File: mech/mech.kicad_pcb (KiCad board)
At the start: 2 copper layers, 53.3 x 78.7 mm, 28 parts, among them P1 Pump_Motor_DC, P2 Pump_Motor_DC, T1 DS18B20, T2 DS18B20, U1 DHT22

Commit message: fix edge corner
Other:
- outline, holes or cut-outs redrawn
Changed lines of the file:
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@@
   )
   (layers
-    (0 F.Cu signal hide)
-    (31 B.Cu signal hide)
+    (0 F.Cu signal)
+    (31 B.Cu signal)
     (32 B.Adhes user)
     (33 F.Adhes user)
@@
       (outputformat 1)
       (mirror false)
-      (drillshape 1)
+      (drillshape 0)
       (scaleselection 1)
       (outputdirectory ""))
@@
     )
   )
+  (gr_arc (start 86.36 184.15) (end 81.28 184.15) (angle -90) (layer Edge.Cuts) (width 0.05))
+  (gr_line (start 129.54 189.23) (end 86.36 189.23) (layer Edge.Cuts) (width 0.05))
+  (gr_line (start 134.62 115.57) (end 134.62 184.15) (layer Edge.Cuts) (width 0.05))
+  (gr_line (start 86.36 110.49) (end 129.54 110.49) (layer Edge.Cuts) (width 0.05))
+  (gr_line (start 81.28 184.15) (end 81.28 115.57) (layer Edge.Cuts) (width 0.05))
+  (gr_arc (start 86.36 115.57) (end 86.36 110.49) (angle -90) (layer Edge.Cuts) (width 0.05))
+  (gr_arc (start 129.54 184.15) (end 129.54 189.23) (angle -90) (layer Edge.Cuts) (width 0.05))
+  (gr_arc (start 129.54 115.57) (end 134.62 115.57) (angle -90) (layer Edge.Cuts) (width 0.05))
   (dimension 78.74 (width 0.12) (layer B.SilkS)
-    (gr_text "78,740 mm" (at 143.51 149.86 90) (layer B.SilkS)
-      (effects (font (size 1 1) (thickness 0.15)))
-    )
-    (feature1 (pts (xy 130.81 110.49) (xy 142.826421 110.49)))
-    (feature2 (pts (xy 130.81 189.23) (xy 142.826421 189.23)))
-    (crossbar (pts (xy 142.24 189.23) (xy 142.24 110.49)))
-    (arrow1a (pts (xy 142.24 110.49) (xy 142.826421 111.616504)))
-    (arrow1b (pts (xy 142.24 110.49) (xy 141.653579 111.616504)))
-    (arrow2a (pts (xy 142.24 189.23) (xy 142.826421 188.103496)))
-    (arrow2b (pts (xy 142.24 189.23) (xy 141.653579 188.103496)))
+    (gr_text "78,740 mm" (at 142.24 149.86 90) (layer B.SilkS)
+      (effects (font (size 1 1) (thickness 0.15)))
+    )
+    (feature1 (pts (xy 129.54 110.49) (xy 141.556421 110.49)))
+    (feature2 (pts (xy 129.54 189.23) (xy 141.556421 189.23)))
+    (crossbar (pts (xy 140.97 189.23) (xy 140.97 110.49)))
+    (arrow1a (pts (xy 140.97 110.49) (xy 141.556421 111.616504)))
+    (arrow1b (pts (xy 140.97 110.49) (xy 140.383579 111.616504)))
+    (arrow2a (pts (xy 140.97 189.23) (xy 141.556421 188.103496)))
+    (arrow2b (pts (xy 140.97 189.23) (xy 140.383579 188.103496)))
   )
   (dimension 53.34 (width 0.12) (layer B.SilkS)
-    (gr_text "53,340 mm" (at 107.95 196.215) (layer B.SilkS)
-      (effects (font (size 1 1) (thickness 0.15)))
-    )
-    (feature1 (pts (xy 134.62 185.42) (xy 134.62 195.531421)))
-    (feature2 (pts (xy 81.28 185.42) (xy 81.28 195.531421)))
-    (crossbar (pts (xy 81.28 194.945) (xy 134.62 194.945)))
-    (arrow1a (pts (xy 134.62 194.945) (xy 133.493496 195.531421)))
-    (arrow1b (pts (xy 134.62 194.945) (xy 133.493496 194.358579)))
-    (arrow2a (pts (xy 81.28 194.945) (xy 82.406504 195.531421)))
-    (arrow2b (pts (xy 81.28 194.945) (xy 82.406504 194.358579)))
-  )
-  (gr_line (start 130.925 110.49) (end 85.205 110.49) (layer Edge.Cuts) (width 0.05))
-  (gr_arc (start 85.09 114.3) (end 85.09 110.49) (angle -90) (layer Edge.Cuts) (width 0.05))
-  (gr_line (start 81.28 185.42) (end 81.28 114.3) (layer Edge.Cuts) (width 0.05))
-  (gr_line (start 130.81 189.23) (end 85.09 189.23) (layer Edge.Cuts) (width 0.05))
-  (gr_arc (start 130.81 185.42) (end 130.81 189.23) (angle -90) (layer Edge.Cuts) (width 0.05))
-  (gr_line (start 134.62 114.3) (end 134.62 185.42) (layer Edge.Cuts) (width 0.05))
-  (gr_arc (start 130.81 114.3) (end 134.62 114.3) (angle -90) (layer Edge.Cuts) (width 0.05))
-  (gr_arc (start 85.09 185.42) (end 81.28 185.42) (angle -90) (layer Edge.Cuts) (width 0.05))
-  (gr_text contact@yasiu.pl (at 108.065 186.055) (layer F.SilkS)
+    (gr_text "53,340 mm" (at 107.95 194.945) (layer B.SilkS)
+      (effects (font (size 1 1) (thickness 0.15)))
+    )
+    (feature1 (pts (xy 134.62 184.15) (xy 134.62 194.261421)))
+    (feature2 (pts (xy 81.28 184.15) (xy 81.28 194.261421)))
+    (crossbar (pts (xy 81.28 193.675) (xy 134.62 193.675)))
+    (arrow1a (pts (xy 134.62 193.675) (xy 133.493496 194.261421)))
+    (arrow1b (pts (xy 134.62 193.675) (xy 133.493496 193.088579)))
+    (arrow2a (pts (xy 81.28 193.675) (xy 82.406504 194.261421)))
+    (arrow2b (pts (xy 81.28 193.675) (xy 82.406504 193.088579)))
+  )
+  (gr_text contact@yasiu.pl (at 108.065 184.785) (layer F.SilkS)
     (effects (font (size 1 1) (thickness 0.15)))
   )

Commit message: add JLC part number stub
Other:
- board text added: "JLCJLCJLCJLC"
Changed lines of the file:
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@@
   (general
     (thickness 1.6)
-    (drawings 13)
+    (drawings 14)
     (tracks 72)
     (zones 0)
@@
     )
   )
+  (gr_text JLCJLCJLCJLC (at 107.95 184.15) (layer B.SilkS)
+    (effects (font (size 1 1) (thickness 0.15)) (justify mirror))
+  )
   (gr_arc (start 86.36 184.15) (end 81.28 184.15) (angle -90) (layer Edge.Cuts) (width 0.05))

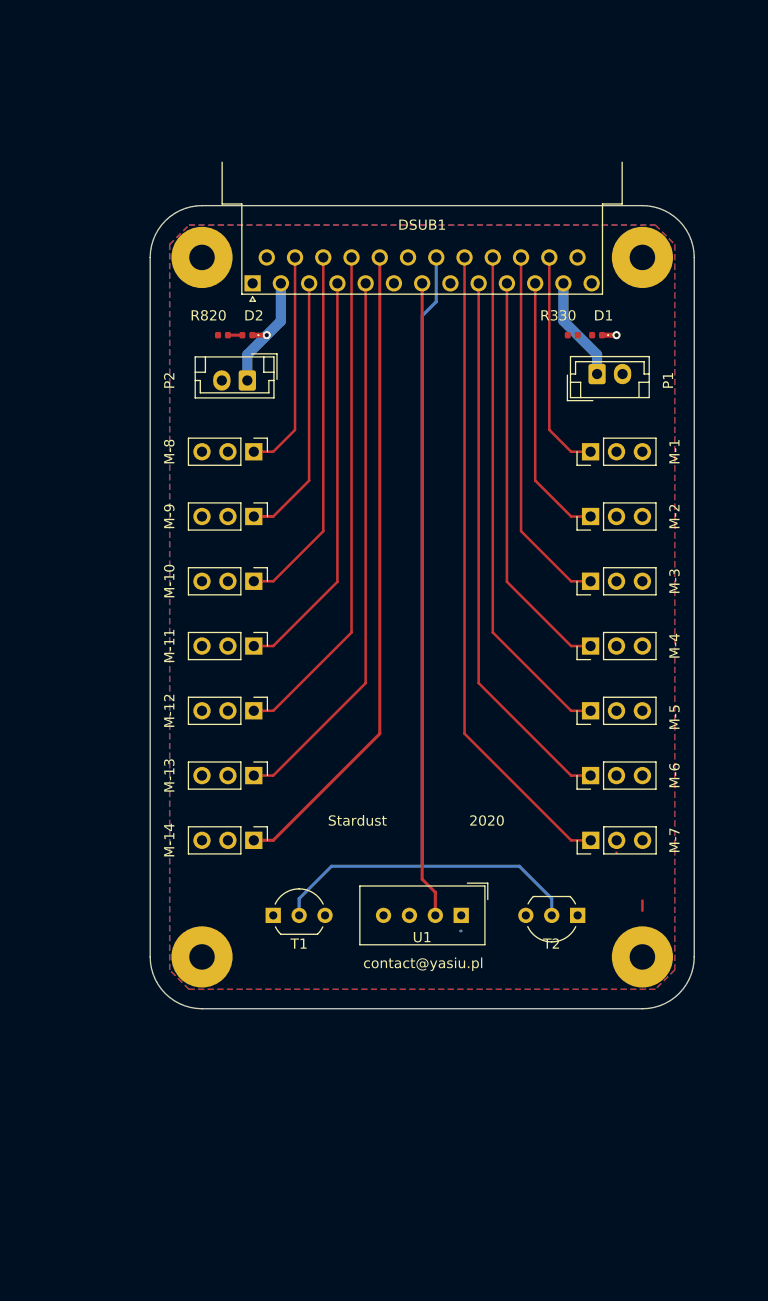
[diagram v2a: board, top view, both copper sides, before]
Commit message: ADC + PCA9685 version
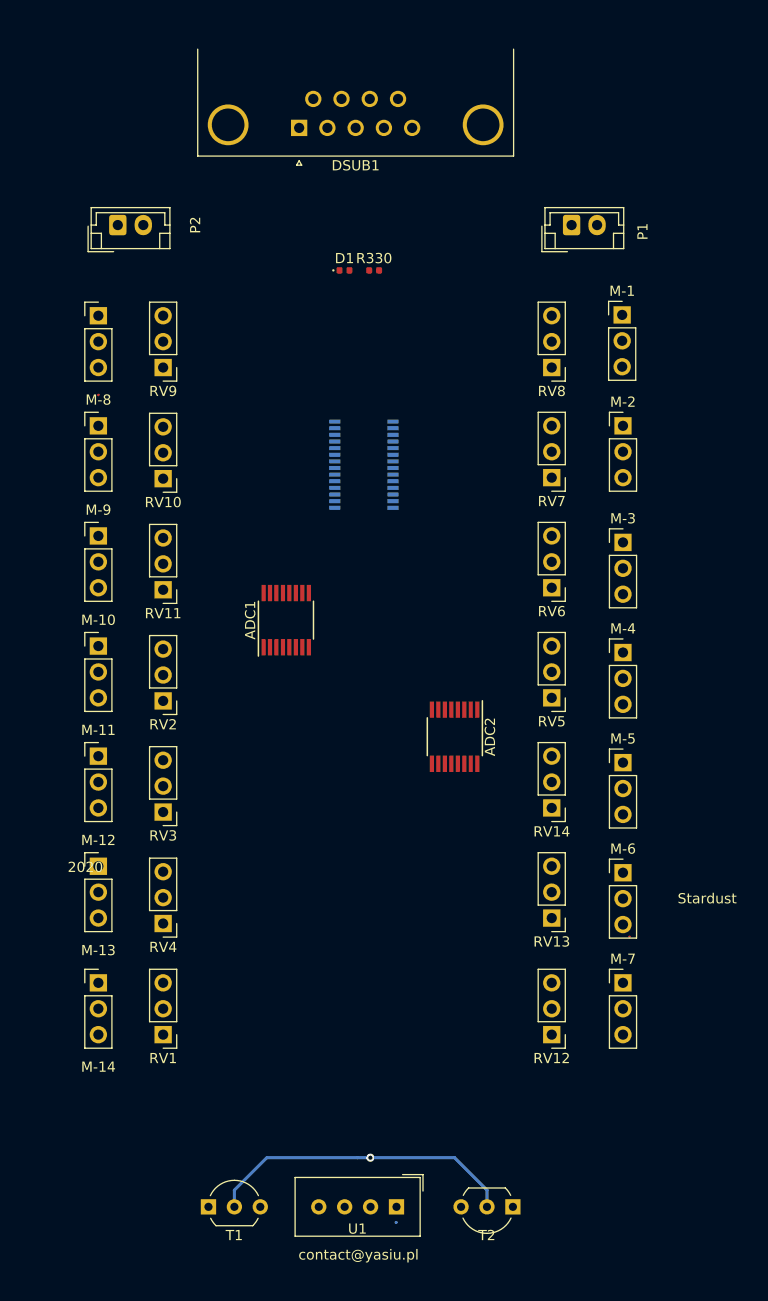
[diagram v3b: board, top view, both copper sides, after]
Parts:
- removed D2: LED, LED_SMD:LED_0402_1005Metric
- removed R820: R, Resistor_SMD:R_0402_1005Metric
- removed REF** (x4): SolderWirePad_1x01_Drill2.5mm, Connector_Wire:SolderWirePad_1x01_Drill2.5mm
- added ADC1: MAX11615, Package_SO:QSOP-16_3.9x4.9mm_P0.635mm, F.Cu at (94.6, 151.1)
- added ADC2: MAX11615, Package_SO:QSOP-16_3.9x4.9mm_P0.635mm, F.Cu at (111.1, 162.6)
- added RV1: R_POT, Connector_PinHeader_2.54mm:PinHeader_1x03_P2.54mm_Vertical, F.Cu at (82.5, 191.8)
- added RV10: R_POT, Connector_PinHeader_2.54mm:PinHeader_1x03_P2.54mm_Vertical, F.Cu at (82.5, 137.3)
- added RV11: R_POT, Connector_PinHeader_2.54mm:PinHeader_1x03_P2.54mm_Vertical, F.Cu at (82.5, 148.2)
- added RV12: R_POT, Connector_PinHeader_2.54mm:PinHeader_1x03_P2.54mm_Vertical, F.Cu at (120.7, 191.8)
- added RV13: R_POT, Connector_PinHeader_2.54mm:PinHeader_1x03_P2.54mm_Vertical, F.Cu at (120.7, 180.3)
- added RV14: R_POT, Connector_PinHeader_2.54mm:PinHeader_1x03_P2.54mm_Vertical, F.Cu at (120.7, 169.5)
- added RV2: R_POT, Connector_PinHeader_2.54mm:PinHeader_1x03_P2.54mm_Vertical, F.Cu at (82.5, 159.1)
- added RV3: R_POT, Connector_PinHeader_2.54mm:PinHeader_1x03_P2.54mm_Vertical, F.Cu at (82.5, 169.9)
- added RV4: R_POT, Connector_PinHeader_2.54mm:PinHeader_1x03_P2.54mm_Vertical, F.Cu at (82.5, 180.9)
- added RV5: R_POT, Connector_PinHeader_2.54mm:PinHeader_1x03_P2.54mm_Vertical, F.Cu at (120.7, 158.8)
- added RV6: R_POT, Connector_PinHeader_2.54mm:PinHeader_1x03_P2.54mm_Vertical, F.Cu at (120.7, 148.0)
- added RV7: R_POT, Connector_PinHeader_2.54mm:PinHeader_1x03_P2.54mm_Vertical, F.Cu at (120.7, 137.2)
- added RV8: R_POT, Connector_PinHeader_2.54mm:PinHeader_1x03_P2.54mm_Vertical, F.Cu at (120.7, 126.4)
- added RV9: R_POT, Connector_PinHeader_2.54mm:PinHeader_1x03_P2.54mm_Vertical, F.Cu at (82.5, 126.4)
- added U2: PCA9685PW, Package_SO:TSSOP-28_4.4x9.7mm_P0.65mm, B.Cu at (102.2, 135.9)
- DSUB1: value DB25_Female -> DB9_Female; footprint Connector_Dsub:DSUB-25_Female_Horizontal_P2.77x2.54mm_EdgePinOffset9.40mm -> Connector_Dsub:DSUB-9_Female_Horizontal_P2.77x2.84mm_EdgePinOffset4.94mm_Housed_MountingHolesOffset7.48mm
- moved U1 29.3 mm to (105.4, 208.7)
- moved T1 29.3 mm to (87.0, 208.7)
- moved T2 29.3 mm to (116.8, 208.7)
- moved D1 25.6 mm to (100.3, 116.8), turned to 0 degrees
- moved M-14 20.7 mm to (76.2, 186.7), turned to 0 degrees
- moved R330 20.5 mm to (103.2, 116.8), turned to 0 degrees
- moved M-8 20.3 mm to (76.2, 121.3), turned to 0 degrees
- moved P2 19.8 mm to (78.1, 112.4), turned to 0 degrees
- moved M-13 17.6 mm to (76.2, 175.3), turned to 0 degrees
- moved M-9 17.6 mm to (76.2, 132.1), turned to 0 degrees
- moved DSUB1 15.9 mm to (95.9, 102.9)
- moved M-10 15.9 mm to (76.2, 142.9), turned to 0 degrees
- moved M-12 15.9 mm to (76.2, 164.5), turned to 0 degrees
- moved M-11 15.2 mm to (76.2, 153.7), turned to 0 degrees
- moved P1 14.8 mm to (122.6, 112.4)
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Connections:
- net Net-(DSUB1-Pad2) renamed Pump-1
- DSUB1 pad 3: Net-(DSUB1-Pad3) -> I2C-SDA
- DSUB1 pad 4: Net-(DSUB1-Pad4) -> 1Wire
- DSUB1 pad 5: Net-(DSUB1-Pad5) -> +5V
- DSUB1 pad 6: (no net) -> Pump-2
- DSUB1 pad 7: Net-(DSUB1-Pad7) -> I2C-SCL
- DSUB1 pad 8: (no net) -> DHT22
- DSUB1 pad 9: Net-(DSUB1-Pad9) -> (no net)
- M-1 pad 1: Net-(DSUB1-Pad24) -> Net-(M-1-Pad1)
- M-10 pad 1: Net-(DSUB1-Pad16) -> Net-(M-10-Pad1)
- M-11 pad 1: Net-(DSUB1-Pad4) -> Net-(M-11-Pad1)
- M-12 pad 1: Net-(DSUB1-Pad17) -> Net-(M-12-Pad1)
- M-13 pad 1: Net-(DSUB1-Pad5) -> Net-(M-13-Pad1)
- M-14 pad 1: Net-(DSUB1-Pad18) -> Net-(M-14-Pad1)
- M-2 pad 1: Net-(DSUB1-Pad11) -> Net-(M-2-Pad1)
- M-3 pad 1: Net-(DSUB1-Pad23) -> Net-(M-3-Pad1)
- M-4 pad 1: Net-(DSUB1-Pad10) -> Net-(M-4-Pad1)
- M-5 pad 1: Net-(DSUB1-Pad22) -> Net-(M-5-Pad1)
- M-6 pad 1: Net-(DSUB1-Pad9) -> Net-(M-6-Pad1)
- M-7 pad 1: Net-(DSUB1-Pad21) -> Net-(M-7-Pad1)
- M-8 pad 1: Net-(DSUB1-Pad15) -> Net-(M-8-Pad1)
- M-9 pad 1: Net-(DSUB1-Pad3) -> Net-(M-9-Pad1)
- P1 pad 1: Net-(DSUB1-Pad12) -> Pump-2
- T1 pad 2: Net-(DSUB1-Pad20) -> 1Wire
- T2 pad 2: Net-(DSUB1-Pad20) -> 1Wire
- T2 pad 3: +5V -> (no net)
- U1 pad 2: Net-(DSUB1-Pad7) -> DHT22
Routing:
- net Net-(DSUB1-Pad20): track 90.9 -> 0.00 mm
- net Net-(DSUB1-Pad21): track 63.4 -> 0.00 mm
- net Net-(DSUB1-Pad18): track 63.4 -> 0.00 mm
- net Net-(DSUB1-Pad7): track 62.5 -> 0.00 mm
- net Net-(DSUB1-Pad9): track 53.9 -> 0.00 mm
- net Net-(DSUB1-Pad5): track 53.9 -> 0.00 mm
- net Net-(DSUB1-Pad22): track 49.5 -> 0.00 mm
- net Net-(DSUB1-Pad17): track 49.5 -> 0.00 mm
- net Net-(DSUB1-Pad10): track 40.1 -> 0.00 mm
- net Net-(DSUB1-Pad4): track 40.1 -> 0.00 mm
- net Net-(DSUB1-Pad23): track 35.7 -> 0.00 mm
- net Net-(DSUB1-Pad16): track 35.7 -> 0.00 mm
- net 1Wire: track 0.00 -> 30.7 mm, vias 0 -> 1
- net Net-(DSUB1-Pad11): track 26.2 -> 0.00 mm
- net Net-(DSUB1-Pad3): track 26.2 -> 0.00 mm
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- removed copper zone on B.Cu, net +5V
- removed copper zone on F.Cu, net GND
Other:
- board outline removed
- net class Default: trace_width 0.5 -> 0.25

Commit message: final
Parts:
- removed ADC1, ADC2: MAX11615, Package_SO:QSOP-16_3.9x4.9mm_P0.635mm
- removed D1: LED, LED_SMD:LED_0402_1005Metric
- removed R330: R, Resistor_SMD:R_0402_1005Metric
- removed the RV12 at (120.7, 191.8)
- removed the RV13 at (120.7, 180.3)
- removed the RV14 at (120.7, 169.5)
- removed the RV8 at (120.7, 126.4)
- added  : MountingHole_3.2mm_M3_DIN965_Pad, MountingHole:MountingHole_3.2mm_M3_DIN965_Pad, F.Cu at (74.5, 101.5)
- added  : MountingHole_3.2mm_M3_DIN965_Pad, MountingHole:MountingHole_3.2mm_M3_DIN965_Pad, F.Cu at (74.5, 210.1)
- added  : MountingHole_3.2mm_M3_DIN965_Pad, MountingHole:MountingHole_3.2mm_M3_DIN965_Pad, F.Cu at (128.5, 210.1)
- added  : MountingHole_3.2mm_M3_DIN965_Pad, MountingHole:MountingHole_3.2mm_M3_DIN965_Pad, F.Cu at (128.5, 101.5)
- added C0: C100nF, Resistor_SMD:R_0603_1608Metric, B.Cu at (97.8, 133.3)
- added C1: C100nF, Resistor_SMD:R_0603_1608Metric, F.Cu at (106.0, 173.4)
- added C2: 10nF, Resistor_SMD:R_0603_1608Metric, F.Cu at (106.0, 161.3)
- added C3: 100nF, Resistor_SMD:R_0603_1608Metric, F.Cu at (106.0, 159.4)
- added C4: C100nF, Resistor_SMD:R_0603_1608Metric, F.Cu at (97.4, 161.2)
- added C5: C10nF, Resistor_SMD:R_0603_1608Metric, F.Cu at (97.4, 173.2)
- added C6: C100nF, Resistor_SMD:R_0603_1608Metric, F.Cu at (97.4, 175.1)
- added R10k1: R, Resistor_SMD:R_0603_1608Metric, F.Cu at (105.4, 120.7)
- added R10k2: R, Resistor_SMD:R_0603_1608Metric, F.Cu at (97.8, 120.7)
- added RV1: R_POT, Connector_PinHeader_2.54mm:PinHeader_1x03_P2.54mm_Vertical, F.Cu at (117.5, 130.2)
- added RV2: R_POT, Connector_PinHeader_2.54mm:PinHeader_1x03_P2.54mm_Vertical, F.Cu at (117.5, 141.6)
- added RV3: R_POT, Connector_PinHeader_2.54mm:PinHeader_1x03_P2.54mm_Vertical, F.Cu at (117.5, 153.0)
- added RV4: R_POT, Connector_PinHeader_2.54mm:PinHeader_1x03_P2.54mm_Vertical, F.Cu at (117.5, 164.5)
- added U3: ADC128D818, Package_SO:TSSOP-16_4.4x5mm_P0.65mm, F.Cu at (95.2, 167.6)
- added U4: ADC128D818, Package_SO:TSSOP-16_4.4x5mm_P0.65mm, F.Cu at (108.0, 167.0)
- moved RV7 61.7 mm to (117.5, 198.8)
- moved P2 44.5 mm to (122.6, 113.0), turned to 270 degrees
- moved P1 41.3 mm to (81.3, 113.0), turned to 270 degrees
- moved RV14 39.8 mm to (85.7, 198.8)
- moved RV6 39.5 mm to (117.5, 187.3)
- moved RV11 27.5 mm to (85.7, 164.5)
- moved RV10 26.9 mm to (85.7, 153.0)
- moved RV8 18.3 mm to (85.7, 130.2)
- moved RV13 17.7 mm to (85.7, 187.3)
- moved RV5 17.4 mm to (117.5, 175.9)
- moved M-13 7.01 mm to (75.6, 182.2)
- moved M-14 7.01 mm to (75.6, 193.7)
- moved M-7 6.99 mm to (127.6, 193.7)
- moved M-12 6.38 mm to (75.6, 170.8)
- moved M-6 6.35 mm to (127.6, 182.2)
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- renumbered RV9 to RV10, RV1 to RV11, RV4 to RV12, RV3 to RV13, RV2 to RV14, RV11 to RV8, RV10 to RV9
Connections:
- DSUB1 pad 0: Net-(DSUB1-Pad0) -> GND
- DSUB1 pad 2: Pump-1 -> 1Wire
- DSUB1 pad 3: I2C-SDA -> (no net)
- DSUB1 pad 4: 1Wire -> DHT22
- DSUB1 pad 7: I2C-SCL -> I2C-SDA
- DSUB1 pad 8: DHT22 -> I2C-SCL
- DSUB1 pad 9: (no net) -> Pump-1
- U2 pad 1: (no net) -> GND
- U2 pad 14: (no net) -> GND
- U2 pad 2: (no net) -> GND
- U2 pad 23: (no net) -> GND
- U2 pad 24: (no net) -> GND
- U2 pad 3: (no net) -> GND
- U2 pad 4: (no net) -> GND
- U2 pad 5: (no net) -> GND
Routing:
- net DHT22: track 0.00 -> 111.2 mm
- net 1Wire: track 30.7 -> 136.9 mm
- net I2C-SCL: track 0.00 -> 82.3 mm, vias 0 -> 2
- net I2C-SDA: track 0.00 -> 81.3 mm, vias 0 -> 4
- net Net-(M-7-Pad1): track 0.00 -> 64.6 mm
- net Net-(M-14-Pad1): track 0.00 -> 64.6 mm
- net Net-(M-6-Pad1): track 0.00 -> 53.4 mm
- net Net-(M-13-Pad1): track 0.00 -> 53.4 mm
- net Net-(M-5-Pad1): track 0.00 -> 43.1 mm
- net Net-(M-12-Pad1): track 0.00 -> 43.1 mm
- net Net-(RV1-Pad2): track 0.00 -> 42.8 mm
- net Net-(RV8-Pad2): track 0.00 -> 42.7 mm
- net GND: track 0.02 -> 42.0 mm, vias 0 -> 6
- net Net-(RV2-Pad2): track 0.00 -> 32.2 mm
- net Net-(M-8-Pad1): track 0.00 -> 32.2 mm
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- added copper zone on F.Cu, net +5V
- added copper zone on B.Cu, net GND
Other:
- board outline added: 66 x 120.7 mm
- board text added: "Stardust 2020"
- board text removed: "2020"
- board text removed: "Stardust"
